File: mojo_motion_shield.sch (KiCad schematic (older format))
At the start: 31 parts, among them J1 Conn_01x24, J10 Conn_01x09, J11 Conn_01x09, J12 Conn_01x09, J13 Conn_01x09, J14 Conn_01x04, J15 Conn_01x04, J16 Conn_01x04, J17 Conn_01x04, J18 Conn_01x04, J19 Conn_01x04, J2 Conn_01x24, J20 Conn_01x04, J21 Conn_01x04, J3 Conn_01x04, J4 Conn_01x03, J5 Conn_01x04, J6 Conn_02x04_Odd_Even, J7 Conn_02x04_Odd_Even, P1 MOJO, U2 A4988, U3 A4988, U4 A4988, U5 A4988

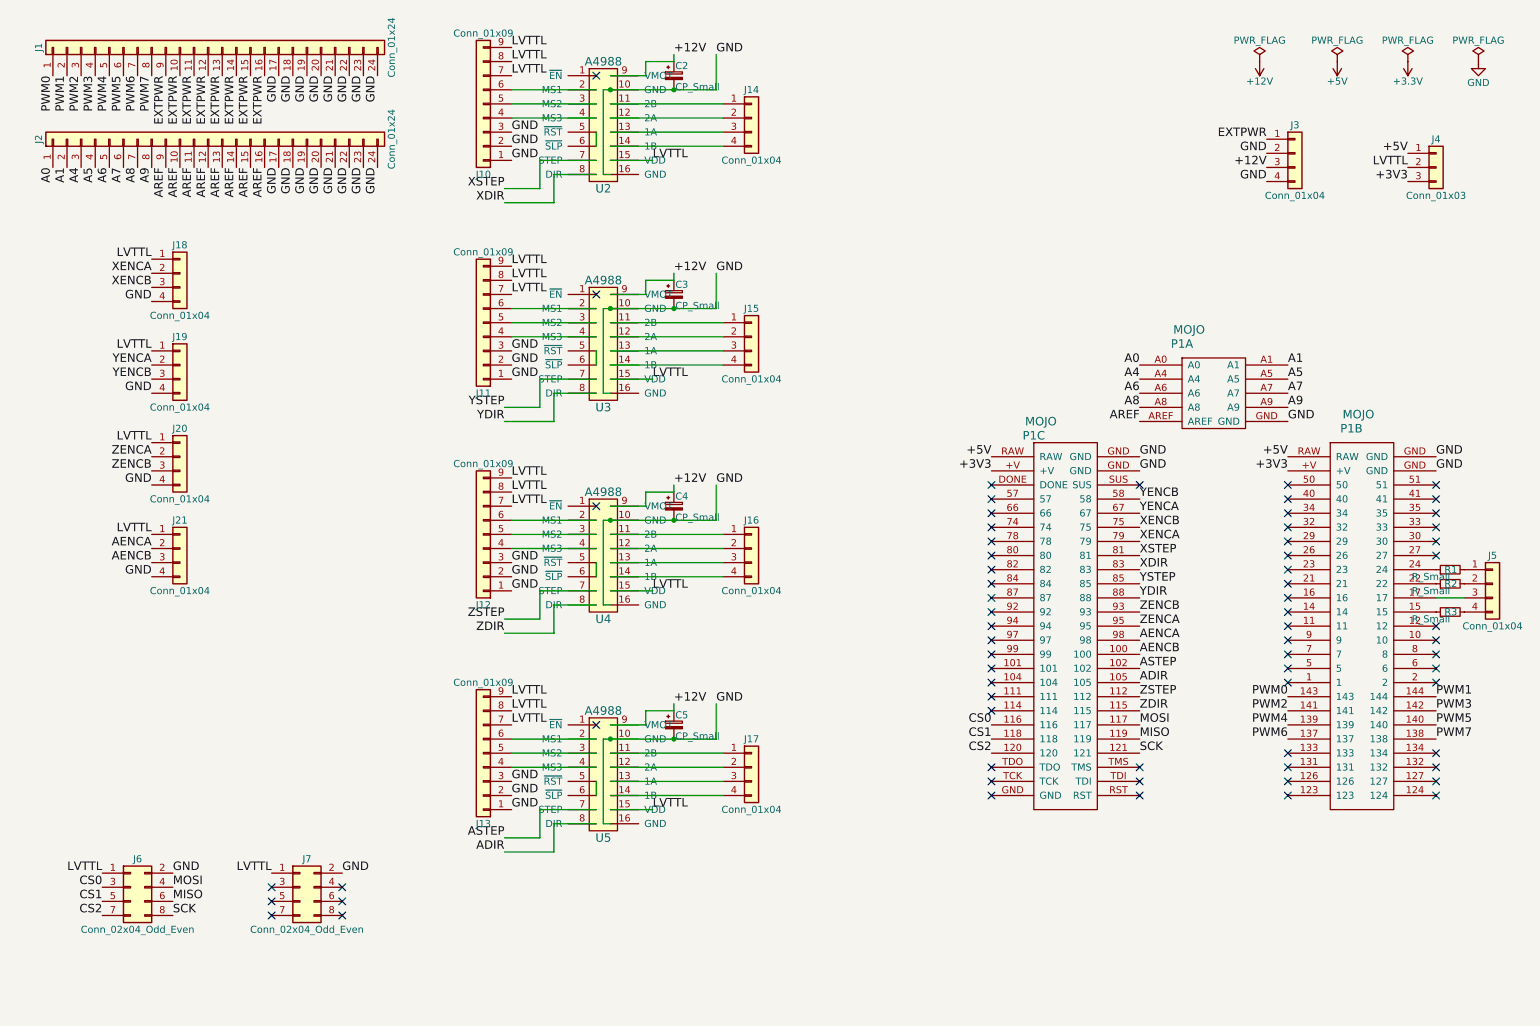
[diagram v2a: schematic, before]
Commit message: implement most of the routes
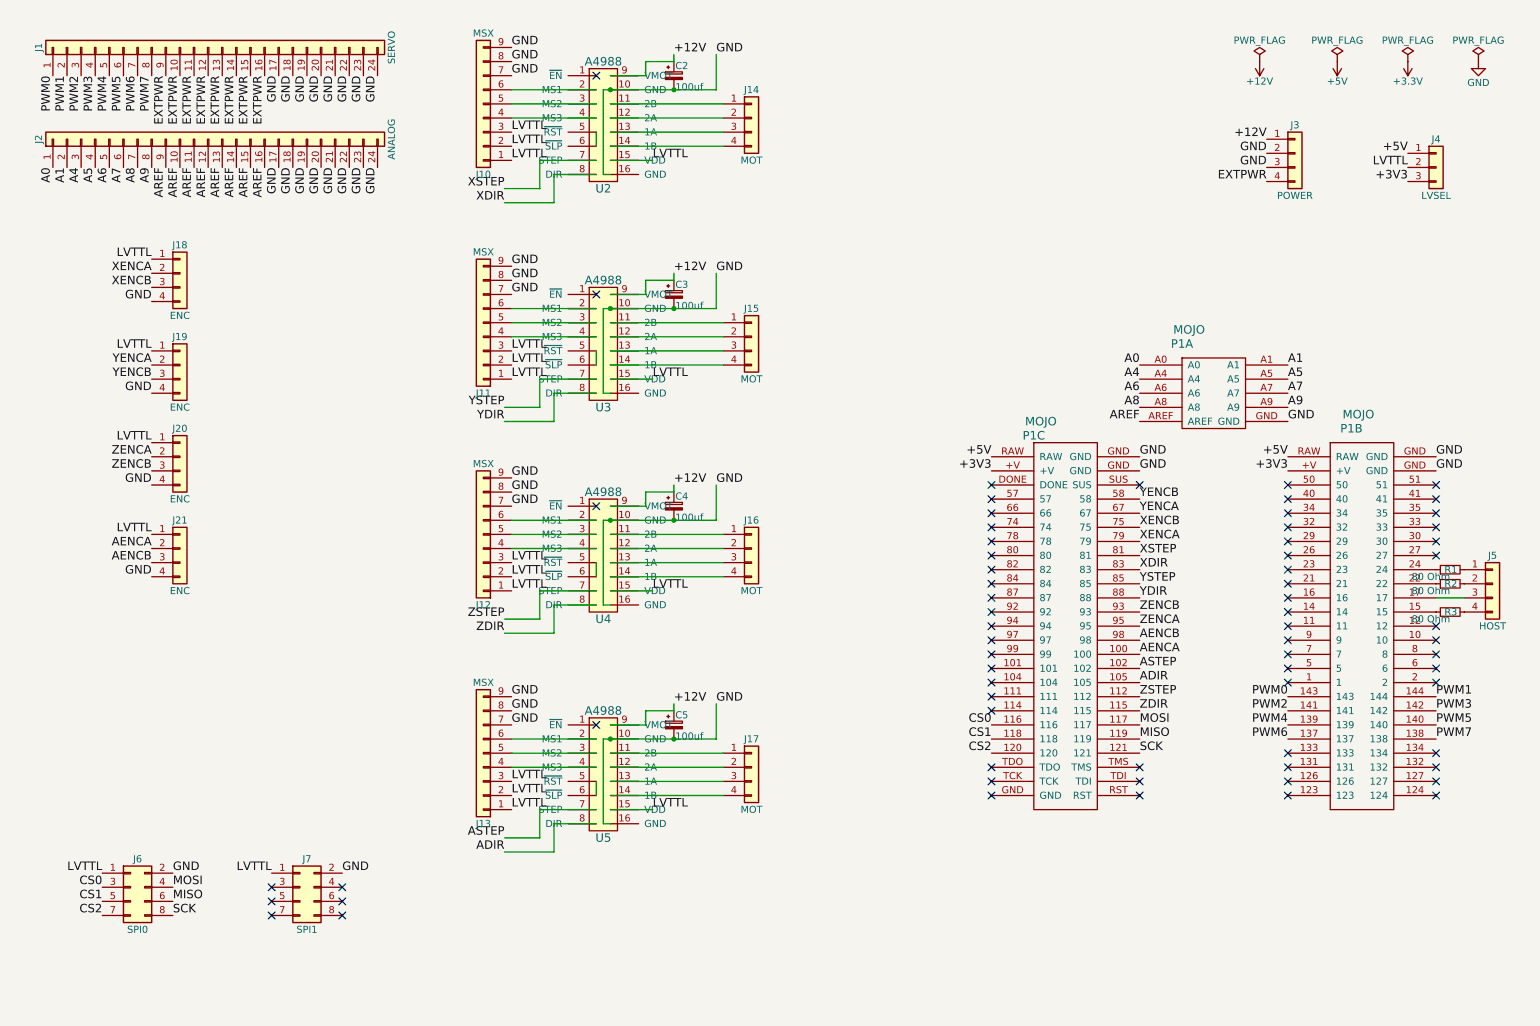
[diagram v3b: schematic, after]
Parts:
- C2, C3, C4, C5: value CP_Small -> 100uf
- J1: value Conn_01x24 -> SERVO
- J10, J11, J12, J13: value Conn_01x09 -> MSX
- J14, J15, J16, J17: value Conn_01x04 -> MOT
- J18, J19, J20, J21: value Conn_01x04 -> ENC
- J2: value Conn_01x24 -> ANALOG
- J3: value Conn_01x04 -> POWER; footprint Pin_Headers:Pin_Header_Straight_1x04_Pitch2.54mm -> mojov3:PhoenixContact_MC-G_04x5.08mm_Angled
- J4: value Conn_01x03 -> LVSEL
- J5: value Conn_01x04 -> HOST; footprint Pin_Headers:Pin_Header_Straight_1x04_Pitch2.54mm -> Pin_Headers:Pin_Header_Angled_1x04_Pitch2.54mm
- J6: value Conn_02x04_Odd_Even -> SPI0
- J7: value Conn_02x04_Odd_Even -> SPI1
- R1, R2, R3: value R_Small -> 80 Ohm
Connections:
- net +12V: now also J3.1 (Pin_1); no longer J3.3 (Pin_3)
- net AENCA: now also P1.100; no longer P1.98
- net AENCB: now also P1.98; no longer P1.100
- net EXTPWR: now also J3.4 (Pin_4); no longer J3.1 (Pin_1)
- net GND: now also J10.7 (Pin_7), J10.8 (Pin_8), J10.9 (Pin_9), J11.7 (Pin_7), J11.8 (Pin_8), J11.9 (Pin_9), J12.7 (Pin_7), J12.8 (Pin_8), J12.9 (Pin_9), J13.7 (Pin_7), J13.8 (Pin_8), J13.9 (Pin_9), J3.3 (Pin_3); no longer J10.1 (Pin_1), J10.2 (Pin_2), J10.3 (Pin_3), J11.1 (Pin_1), J11.2 (Pin_2), J11.3 (Pin_3), J12.1 (Pin_1), J12.2 (Pin_2), J12.3 (Pin_3), J13.1 (Pin_1), J13.2 (Pin_2), J13.3 (Pin_3), J3.4 (Pin_4)
- net LVTTL: now also J10.1 (Pin_1), J10.2 (Pin_2), J10.3 (Pin_3), J11.1 (Pin_1), J11.2 (Pin_2), J11.3 (Pin_3), J12.1 (Pin_1), J12.2 (Pin_2), J12.3 (Pin_3), J13.1 (Pin_1), J13.2 (Pin_2), J13.3 (Pin_3); no longer J10.7 (Pin_7), J10.8 (Pin_8), J10.9 (Pin_9), J11.7 (Pin_7), J11.8 (Pin_8), J11.9 (Pin_9), J12.7 (Pin_7), J12.8 (Pin_8), J12.9 (Pin_9), J13.7 (Pin_7), J13.8 (Pin_8), J13.9 (Pin_9)
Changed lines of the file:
@@
 Text Label 8450 4950 0    60   ~ 0
 ZENCA
+Text Label 8450 5150 0    60   ~ 0
+AENCA
 Text Label 8450 5050 0    60   ~ 0
-AENCA
-Text Label 8450 5150 0    60   ~ 0
 AENCB
 Text Label 8450 5250 0    60   ~ 0
@@
 P 1850 1500
 F 0 "J2" H 1850 2700 50  0000 C CNN
-F 1 "Conn_01x24" H 1850 200 50  0000 C CNN
+F 1 "ANALOG" H 1850 200 50  0000 C CNN
 F 2 "mojov3:Pin_Header_Angled_3x08_Pitch2.54mm" H 1850 1500 50  0001 C CNN
 F 3 "" H 1850 1500 50  0001 C CNN
@@
 P 1850 850
 F 0 "J1" H 1850 2050 50  0000 C CNN
-F 1 "Conn_01x24" H 1850 -450 50  0000 C CNN
+F 1 "SERVO" H 1850 -450 50  0000 C CNN
 F 2 "mojov3:Pin_Header_Angled_3x08_Pitch2.54mm" H 1850 850 50  0001 C CNN
 F 3 "" H 1850 850 50  0001 C CNN
@@
 P 9550 1600
 F 0 "J3" H 9550 1800 50  0000 C CNN
-F 1 "Conn_01x04" H 9550 1300 50  0000 C CNN
-F 2 "Pin_Headers:Pin_Header_Straight_1x04_Pitch2.54mm" H 9550 1600 50  0001 C CNN
+F 1 "POWER" H 9550 1300 50  0000 C CNN
+F 2 "mojov3:PhoenixContact_MC-G_04x5.08mm_Angled" H 9550 1600 50  0001 C CNN
 F 3 "" H 9550 1600 50  0001 C CNN
 	1    9550 1600
@@
 P 10550 1700
 F 0 "J4" H 10550 1900 50  0000 C CNN
-F 1 "Conn_01x03" H 10550 1500 50  0000 C CNN
+F 1 "LVSEL" H 10550 1500 50  0000 C CNN
 F 2 "Pin_Headers:Pin_Header_Straight_1x03_Pitch2.54mm" H 10550 1700 50  0001 C CNN
 F 3 "" H 10550 1700 50  0001 C CNN
@@
 Text Label 2250 1050 3    60   ~ 0
 EXTPWR
-Text Label 9350 1500 2    60   ~ 0
+Text Label 9350 1800 2    60   ~ 0
 EXTPWR
 $Comp
@@
 Text Label 10350 1700 2    60   ~ 0
 LVTTL
-Text Label 9350 1800 2    60   ~ 0
+Text Label 9350 1700 2    60   ~ 0
 GND
 Text Label 9350 1600 2    60   ~ 0
 GND
-Text Label 9350 1700 2    60   ~ 0
+Text Label 9350 1500 2    60   ~ 0
 +12V
 $Comp
@@
 P 1300 6800
 F 0 "J6" H 1350 7000 50  0000 C CNN
-F 1 "Conn_02x04_Odd_Even" H 1350 6500 50  0000 C CNN
+F 1 "SPI0" H 1350 6500 50  0000 C CNN
 F 2 "Pin_Headers:Pin_Header_Straight_2x04_Pitch2.54mm" H 1300 6800 50  0001 C CNN
 F 3 "" H 1300 6800 50  0001 C CNN
@@
 P 2500 6800
 F 0 "J7" H 2550 7000 50  0000 C CNN
-F 1 "Conn_02x04_Odd_Even" H 2550 6500 50  0000 C CNN
+F 1 "SPI1" H 2550 6500 50  0000 C CNN
 F 2 "Pin_Headers:Pin_Header_Straight_2x04_Pitch2.54mm" H 2500 6800 50  0001 C CNN
 F 3 "" H 2500 6800 50  0001 C CNN
@@
 P 10950 4650
 F 0 "J5" H 10950 4850 50  0000 C CNN
-F 1 "Conn_01x04" H 10950 4350 50  0000 C CNN
-F 2 "Pin_Headers:Pin_Header_Straight_1x04_Pitch2.54mm" H 10950 4650 50  0001 C CNN
+F 1 "HOST" H 10950 4350 50  0000 C CNN
+F 2 "Pin_Headers:Pin_Header_Angled_1x04_Pitch2.54mm" H 10950 4650 50  0001 C CNN
 F 3 "" H 10950 4650 50  0001 C CNN
 	1    10950 4650
@@
 P 10650 4850
 F 0 "R3" V 10650 4800 50  0000 L CNN
-F 1 "R_Small" V 10600 4850 50  0000 L CNN
+F 1 "80 Ohm" V 10600 4850 50  0000 L CNN
 F 2 "Resistors_THT:R_Axial_DIN0204_L3.6mm_D1.6mm_P2.54mm_Vertical" H 10650 4850 50  0001 C CNN
 F 3 "" H 10650 4850 50  0001 C CNN
@@
 P 10650 4550
 F 0 "R1" V 10650 4500 50  0000 L CNN
-F 1 "R_Small" V 10600 4550 50  0000 L CNN
+F 1 "80 Ohm" V 10600 4550 50  0000 L CNN
 F 2 "Resistors_THT:R_Axial_DIN0204_L3.6mm_D1.6mm_P2.54mm_Vertical" H 10650 4550 50  0001 C CNN
 F 3 "" H 10650 4550 50  0001 C CNN
@@
 P 10650 4650
 F 0 "R2" V 10650 4600 50  0000 L CNN
-F 1 "R_Small" V 10600 4650 50  0000 L CNN
+F 1 "80 Ohm" V 10600 4650 50  0000 L CNN
 F 2 "Resistors_THT:R_Axial_DIN0204_L3.6mm_D1.6mm_P2.54mm_Vertical" H 10650 4650 50  0001 C CNN
 F 3 "" H 10650 4650 50  0001 C CNN
@@
 P 5150 1050
 F 0 "C2" H 5160 1120 50  0000 L CNN
-F 1 "CP_Small" H 5160 970 50  0000 L CNN
+F 1 "100uf" H 5160 970 50  0000 L CNN
 F 2 "Capacitors_THT:CP_Radial_D5.0mm_P2.50mm" H 5150 1050 50  0001 C CNN
 F 3 "" H 5150 1050 50  0001 C CNN
@@
 P 5700 1350
 F 0 "J14" H 5700 1550 50  0000 C CNN
-F 1 "Conn_01x04" H 5700 1050 50  0000 C CNN
+F 1 "MOT" H 5700 1050 50  0000 C CNN
 F 2 "Pin_Headers:Pin_Header_Straight_1x04_Pitch2.54mm" H 5700 1350 50  0001 C CNN
 F 3 "" H 5700 1350 50  0001 C CNN
@@
 P 3800 1250
 F 0 "J10" H 3800 1750 50  0000 C CNN
-F 1 "Conn_01x09" H 3800 750 50  0000 C CNN
+F 1 "MSX" H 3800 750 50  0000 C CNN
 F 2 "mojov3:Pin_Header_Straight_3x03_Pitch2.54mm" H 3800 1250 50  0001 C CNN
 F 3 "" H 3800 1250 50  0001 C CNN
@@
 	-1   0    0    1
 $EndComp
+Text Label 4000 1050 0    60   ~ 0
+GND
+Text Label 4000 950  0    60   ~ 0
+GND
+Text Label 4000 850  0    60   ~ 0
+GND
 Text Label 4000 1650 0    60   ~ 0
-GND
+LVTTL
 Text Label 4000 1550 0    60   ~ 0
-GND
+LVTTL
 Text Label 4000 1450 0    60   ~ 0
-GND
-Text Label 4000 1050 0    60   ~ 0
-LVTTL
-Text Label 4000 950  0    60   ~ 0
-LVTTL
-Text Label 4000 850  0    60   ~ 0
 LVTTL
 Wire Wire Line
@@
 P 5150 2600
 F 0 "C3" H 5160 2670 50  0000 L CNN
-F 1 "CP_Small" H 5160 2520 50  0000 L CNN
+F 1 "100uf" H 5160 2520 50  0000 L CNN
 F 2 "Capacitors_THT:CP_Radial_D5.0mm_P2.50mm" H 5150 2600 50  0001 C CNN
 F 3 "" H 5150 2600 50  0001 C CNN
@@
 P 5700 2900
 F 0 "J15" H 5700 3100 50  0000 C CNN
-F 1 "Conn_01x04" H 5700 2600 50  0000 C CNN
+F 1 "MOT" H 5700 2600 50  0000 C CNN
 F 2 "Pin_Headers:Pin_Header_Straight_1x04_Pitch2.54mm" H 5700 2900 50  0001 C CNN
 F 3 "" H 5700 2900 50  0001 C CNN
@@
 P 3800 2800
 F 0 "J11" H 3800 3300 50  0000 C CNN
-F 1 "Conn_01x09" H 3800 2300 50  0000 C CNN
+F 1 "MSX" H 3800 2300 50  0000 C CNN
 F 2 "mojov3:Pin_Header_Straight_3x03_Pitch2.54mm" H 3800 2800 50  0001 C CNN
 F 3 "" H 3800 2800 50  0001 C CNN
@@
 	-1   0    0    1
 $EndComp
+Text Label 4000 2600 0    60   ~ 0
+GND
+Text Label 4000 2500 0    60   ~ 0
+GND
+Text Label 4000 2400 0    60   ~ 0
+GND
 Text Label 4000 3200 0    60   ~ 0
-GND
+LVTTL
 Text Label 4000 3100 0    60   ~ 0
-GND
+LVTTL
 Text Label 4000 3000 0    60   ~ 0
-GND
-Text Label 4000 2600 0    60   ~ 0
-LVTTL
-Text Label 4000 2500 0    60   ~ 0
-LVTTL
-Text Label 4000 2400 0    60   ~ 0
 LVTTL
 Wire Wire Line
@@
 P 5150 4100
 F 0 "C4" H 5160 4170 50  0000 L CNN
-F 1 "CP_Small" H 5160 4020 50  0000 L CNN
+F 1 "100uf" H 5160 4020 50  0000 L CNN
 F 2 "Capacitors_THT:CP_Radial_D5.0mm_P2.50mm" H 5150 4100 50  0001 C CNN
 F 3 "" H 5150 4100 50  0001 C CNN
@@
 P 5700 4400
 F 0 "J16" H 5700 4600 50  0000 C CNN
-F 1 "Conn_01x04" H 5700 4100 50  0000 C CNN
+F 1 "MOT" H 5700 4100 50  0000 C CNN
 F 2 "Pin_Headers:Pin_Header_Straight_1x04_Pitch2.54mm" H 5700 4400 50  0001 C CNN
 F 3 "" H 5700 4400 50  0001 C CNN
@@
 P 3800 4300
 F 0 "J12" H 3800 4800 50  0000 C CNN
-F 1 "Conn_01x09" H 3800 3800 50  0000 C CNN
+F 1 "MSX" H 3800 3800 50  0000 C CNN
 F 2 "mojov3:Pin_Header_Straight_3x03_Pitch2.54mm" H 3800 4300 50  0001 C CNN
 F 3 "" H 3800 4300 50  0001 C CNN
@@
 	-1   0    0    1
 $EndComp
+Text Label 4000 4100 0    60   ~ 0
+GND
+Text Label 4000 4000 0    60   ~ 0
+GND
+Text Label 4000 3900 0    60   ~ 0
+GND
 Text Label 4000 4700 0    60   ~ 0
-GND
+LVTTL
 Text Label 4000 4600 0    60   ~ 0
-GND
+LVTTL
 Text Label 4000 4500 0    60   ~ 0
-GND
-Text Label 4000 4100 0    60   ~ 0
-LVTTL
-Text Label 4000 4000 0    60   ~ 0
-LVTTL
-Text Label 4000 3900 0    60   ~ 0
 LVTTL
 Wire Wire Line
@@
 P 5150 5650
 F 0 "C5" H 5160 5720 50  0000 L CNN
-F 1 "CP_Small" H 5160 5570 50  0000 L CNN
+F 1 "100uf" H 5160 5570 50  0000 L CNN
 F 2 "Capacitors_THT:CP_Radial_D5.0mm_P2.50mm" H 5150 5650 50  0001 C CNN
 F 3 "" H 5150 5650 50  0001 C CNN
@@
 P 5700 5950
 F 0 "J17" H 5700 6150 50  0000 C CNN
-F 1 "Conn_01x04" H 5700 5650 50  0000 C CNN
+F 1 "MOT" H 5700 5650 50  0000 C CNN
 F 2 "Pin_Headers:Pin_Header_Straight_1x04_Pitch2.54mm" H 5700 5950 50  0001 C CNN
 F 3 "" H 5700 5950 50  0001 C CNN
@@
 P 3800 5850
 F 0 "J13" H 3800 6350 50  0000 C CNN
-F 1 "Conn_01x09" H 3800 5350 50  0000 C CNN
+F 1 "MSX" H 3800 5350 50  0000 C CNN
 F 2 "mojov3:Pin_Header_Straight_3x03_Pitch2.54mm" H 3800 5850 50  0001 C CNN
 F 3 "" H 3800 5850 50  0001 C CNN
@@
 	-1   0    0    1
 $EndComp
+Text Label 4000 5650 0    60   ~ 0
+GND
+Text Label 4000 5550 0    60   ~ 0
+GND
+Text Label 4000 5450 0    60   ~ 0
+GND
 Text Label 4000 6250 0    60   ~ 0
-GND
+LVTTL
 Text Label 4000 6150 0    60   ~ 0
-GND
+LVTTL
 Text Label 4000 6050 0    60   ~ 0
-GND
-Text Label 4000 5650 0    60   ~ 0
-LVTTL
-Text Label 4000 5550 0    60   ~ 0
-LVTTL
-Text Label 4000 5450 0    60   ~ 0
 LVTTL
 Wire Wire Line
@@
 P 1650 2450
 F 0 "J18" H 1650 2650 50  0000 C CNN
-F 1 "Conn_01x04" H 1650 2150 50  0000 C CNN
+F 1 "ENC" H 1650 2150 50  0000 C CNN
 F 2 "Pin_Headers:Pin_Header_Straight_1x04_Pitch2.54mm" H 1650 2450 50  0001 C CNN
 F 3 "" H 1650 2450 50  0001 C CNN
@@
 P 1650 3100
 F 0 "J19" H 1650 3300 50  0000 C CNN
-F 1 "Conn_01x04" H 1650 2800 50  0000 C CNN
+F 1 "ENC" H 1650 2800 50  0000 C CNN
 F 2 "Pin_Headers:Pin_Header_Straight_1x04_Pitch2.54mm" H 1650 3100 50  0001 C CNN
 F 3 "" H 1650 3100 50  0001 C CNN
@@
 P 1650 3750
 F 0 "J20" H 1650 3950 50  0000 C CNN
-F 1 "Conn_01x04" H 1650 3450 50  0000 C CNN
+F 1 "ENC" H 1650 3450 50  0000 C CNN
 F 2 "Pin_Headers:Pin_Header_Straight_1x04_Pitch2.54mm" H 1650 3750 50  0001 C CNN
 F 3 "" H 1650 3750 50  0001 C CNN
@@
 P 1650 4400
 F 0 "J21" H 1650 4600 50  0000 C CNN
-F 1 "Conn_01x04" H 1650 4100 50  0000 C CNN
+F 1 "ENC" H 1650 4100 50  0000 C CNN
 F 2 "Pin_Headers:Pin_Header_Straight_1x04_Pitch2.54mm" H 1650 4400 50  0001 C CNN
 F 3 "" H 1650 4400 50  0001 C CNN
